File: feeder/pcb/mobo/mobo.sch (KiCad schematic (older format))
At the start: 43 parts, among them J1 SPRING_FINGER_INTERFACE, J3 SWD_10, M1 DRIVE_MOTOR, M2 PEEL_MOTOR, SW1 BUTTON_1, SW2 BUTTON_2, SW3 RESET_BUTTON, SW4 TAPE_DETECT, SW5 FILM_TENSION, U1 STM32F030K6Tx, U2 VCNT2020, U3 MAX3485, U4 DRV8833PW, U5 AP1117-33, Y1 Crystal_GND24_Small

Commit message: layout and routing done, silkscreen placed. passing drc.
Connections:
- net FILM_TENSION: now also SW5.3 (C); no longer SW5.2 (B)
- net GND: now also SW4.1 (A), SW5.1 (A); no longer SW4.3 (C), SW5.3 (C)
- net LED2: no longer U1.18 (PA8)
- net SLOT_DETECT: no longer U1.7 (PA1)
- net TAPE_DETECT: now also SW4.3 (C); no longer SW4.2 (B)
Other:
- moved on the sheet: SW4, SW5
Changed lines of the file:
@@
 L Switch:SW_SPDT SW4
 U 1 1 5DC9EA90
-P 4000 7050
-F 0 "SW4" H 4000 7335 50  0000 C CNN
-F 1 "TAPE_DETECT" H 4000 7244 50  0000 C CNN
-F 2 "index:K5-1624SA-01" H 4000 7050 50  0001 C CNN
-F 3 "" H 4000 7050 50  0001 C CNN
-	1    4000 7050
-	1    0    0    -1
+P 4100 6750
+F 0 "SW4" V 4025 6925 50  0000 C CNN
+F 1 "TAPE_DETECT" V 3925 7100 50  0000 C CNN
+F 2 "index:K5-1624SA-01" H 4100 6750 50  0001 C CNN
+F 3 "" H 4100 6750 50  0001 C CNN
+	1    4100 6750
+	0    1    1    0
 $EndComp
 $Comp
@@
 	1    0    0    -1
 $EndComp
-Wire Wire Line
-	4200 7150 4400 7150
-Wire Wire Line
-	4400 7150 4400 7300
 Wire Wire Line
 	3700 7050 3750 7050
@@
 	3750 7300 3750 7050
 Connection ~ 3750 7050
-Wire Wire Line
-	3750 7050 3800 7050
 $Comp
 L Switch:SW_Push SW3
@@
 $EndComp
 Connection ~ 3850 1150
-Text GLabel 4450 2150 2    50   Input ~ 0
-LED2
 Wire Wire Line
 	3950 1150 4050 1150
@@
 Text Notes 4800 4775 0    50   ~ 0
 POWER
-Text GLabel 4450 1450 2    50   Input ~ 0
-SLOT_DETECT
 $Comp
 L stephen:TEST TP1
@@
 L Switch:SW_SPDT SW5
 U 1 1 5F6958ED
-P 4025 5650
-F 0 "SW5" H 4025 5935 50  0000 C CNN
-F 1 "FILM_TENSION" H 4025 5844 50  0000 C CNN
-F 2 "index:K5-1624SA-01" H 4025 5650 50  0001 C CNN
-F 3 "" H 4025 5650 50  0001 C CNN
-	1    4025 5650
-	1    0    0    -1
+P 4125 5350
+F 0 "SW5" V 3975 5525 50  0000 C CNN
+F 1 "FILM_TENSION" V 3875 5700 50  0000 C CNN
+F 2 "index:K5-1624SA-01" H 4125 5350 50  0001 C CNN
+F 3 "" H 4125 5350 50  0001 C CNN
+	1    4125 5350
+	0    1    1    0
 $EndComp
 $Comp
@@
 	1    0    0    -1
 $EndComp
-Wire Wire Line
-	4225 5750 4425 5750
-Wire Wire Line
-	4425 5750 4425 5900
 Wire Wire Line
 	3725 5650 3775 5650
@@
 	3775 5900 3775 5650
 Connection ~ 3775 5650
-Wire Wire Line
-	3775 5650 3825 5650
 Text GLabel 3725 5650 0    50   Input ~ 0
 FILM_TENSION
@@
 Wire Wire Line
 	2175 1850 2175 2500
+Wire Wire Line
+	4425 5550 4225 5550
+Wire Wire Line
+	4425 5550 4425 5900
+Wire Wire Line
+	4400 6950 4200 6950
+Wire Wire Line
+	4400 6950 4400 7300
+Wire Wire Line
+	3775 5650 3775 5550
+Wire Wire Line
+	3775 5550 4025 5550
+Wire Wire Line
+	4000 7050 4000 6950
+Wire Wire Line
+	3750 7050 4000 7050
 $EndSCHEMATC

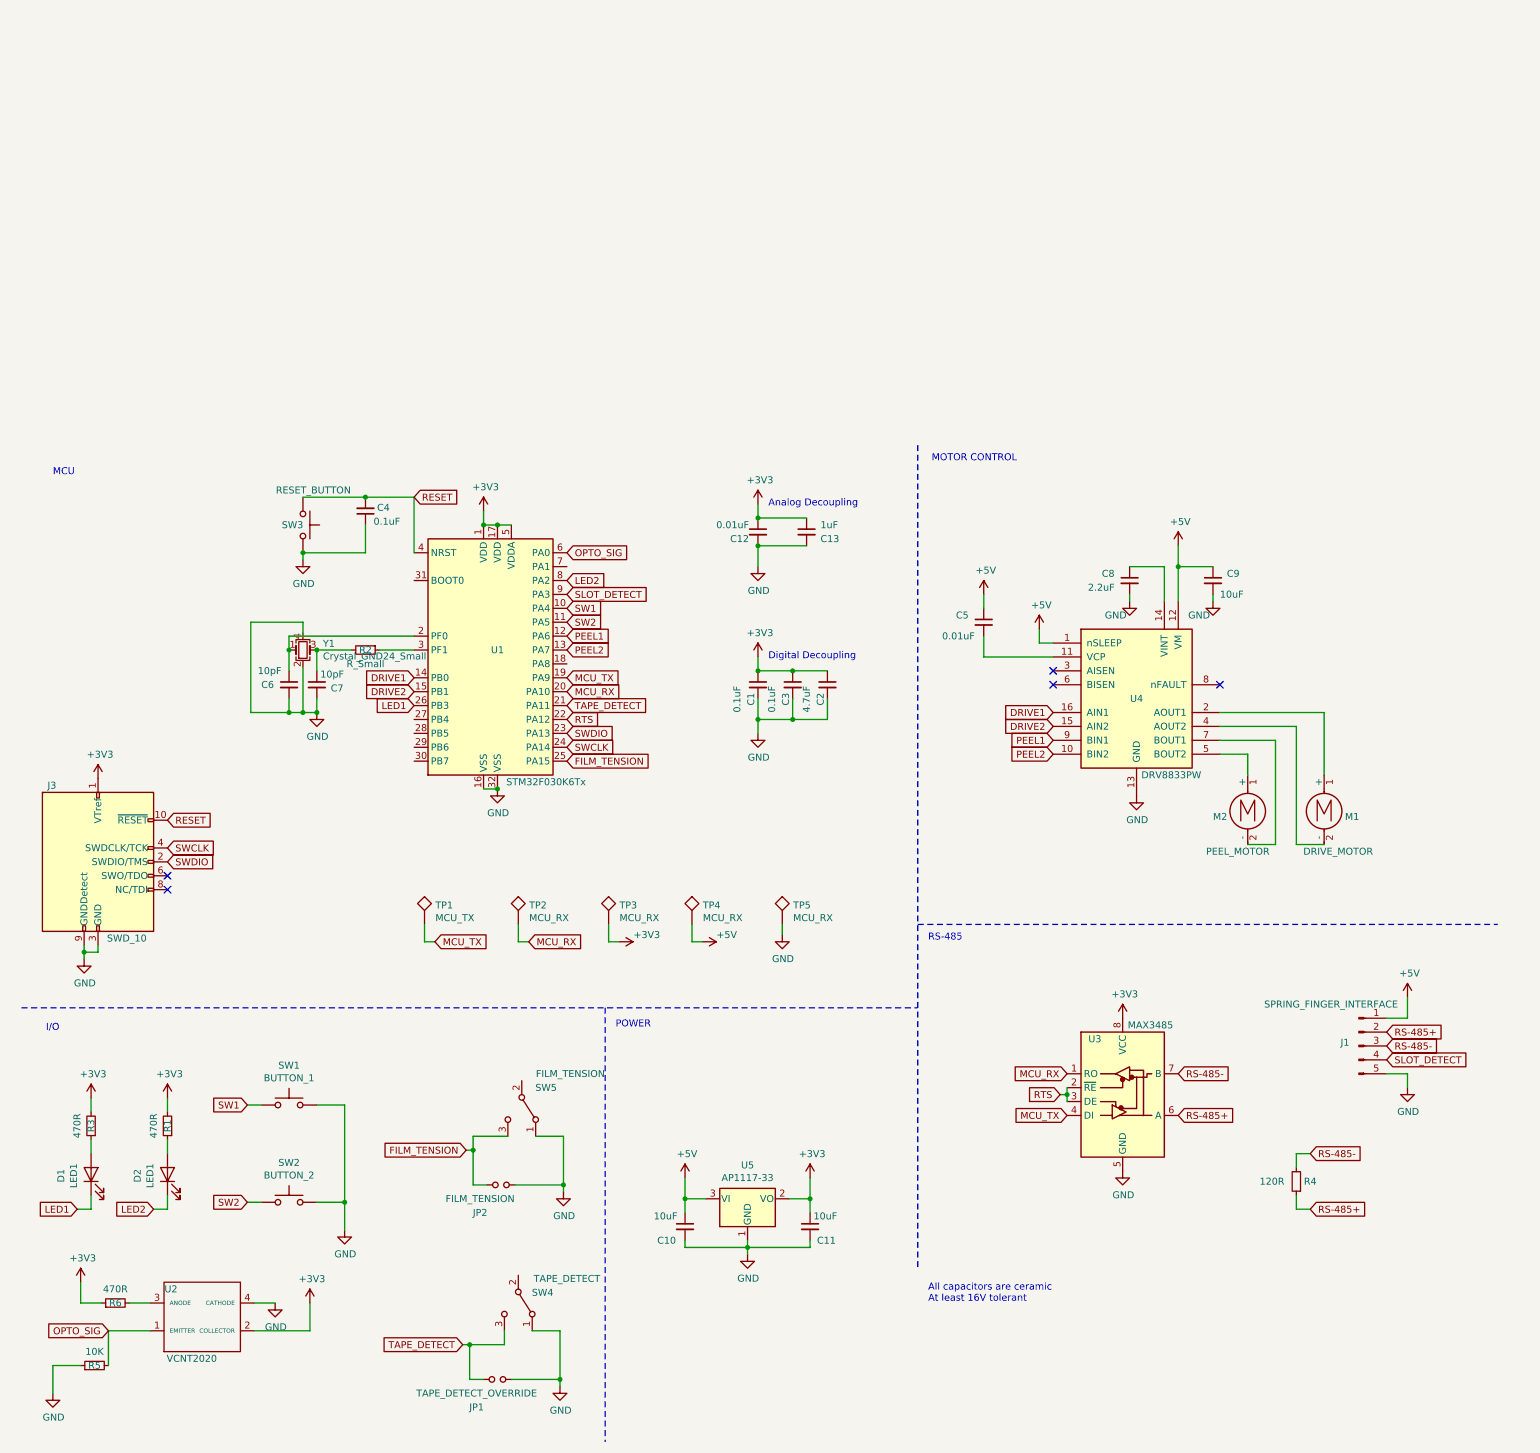
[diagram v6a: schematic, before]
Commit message: pulled DRV8833 sense pins to ground
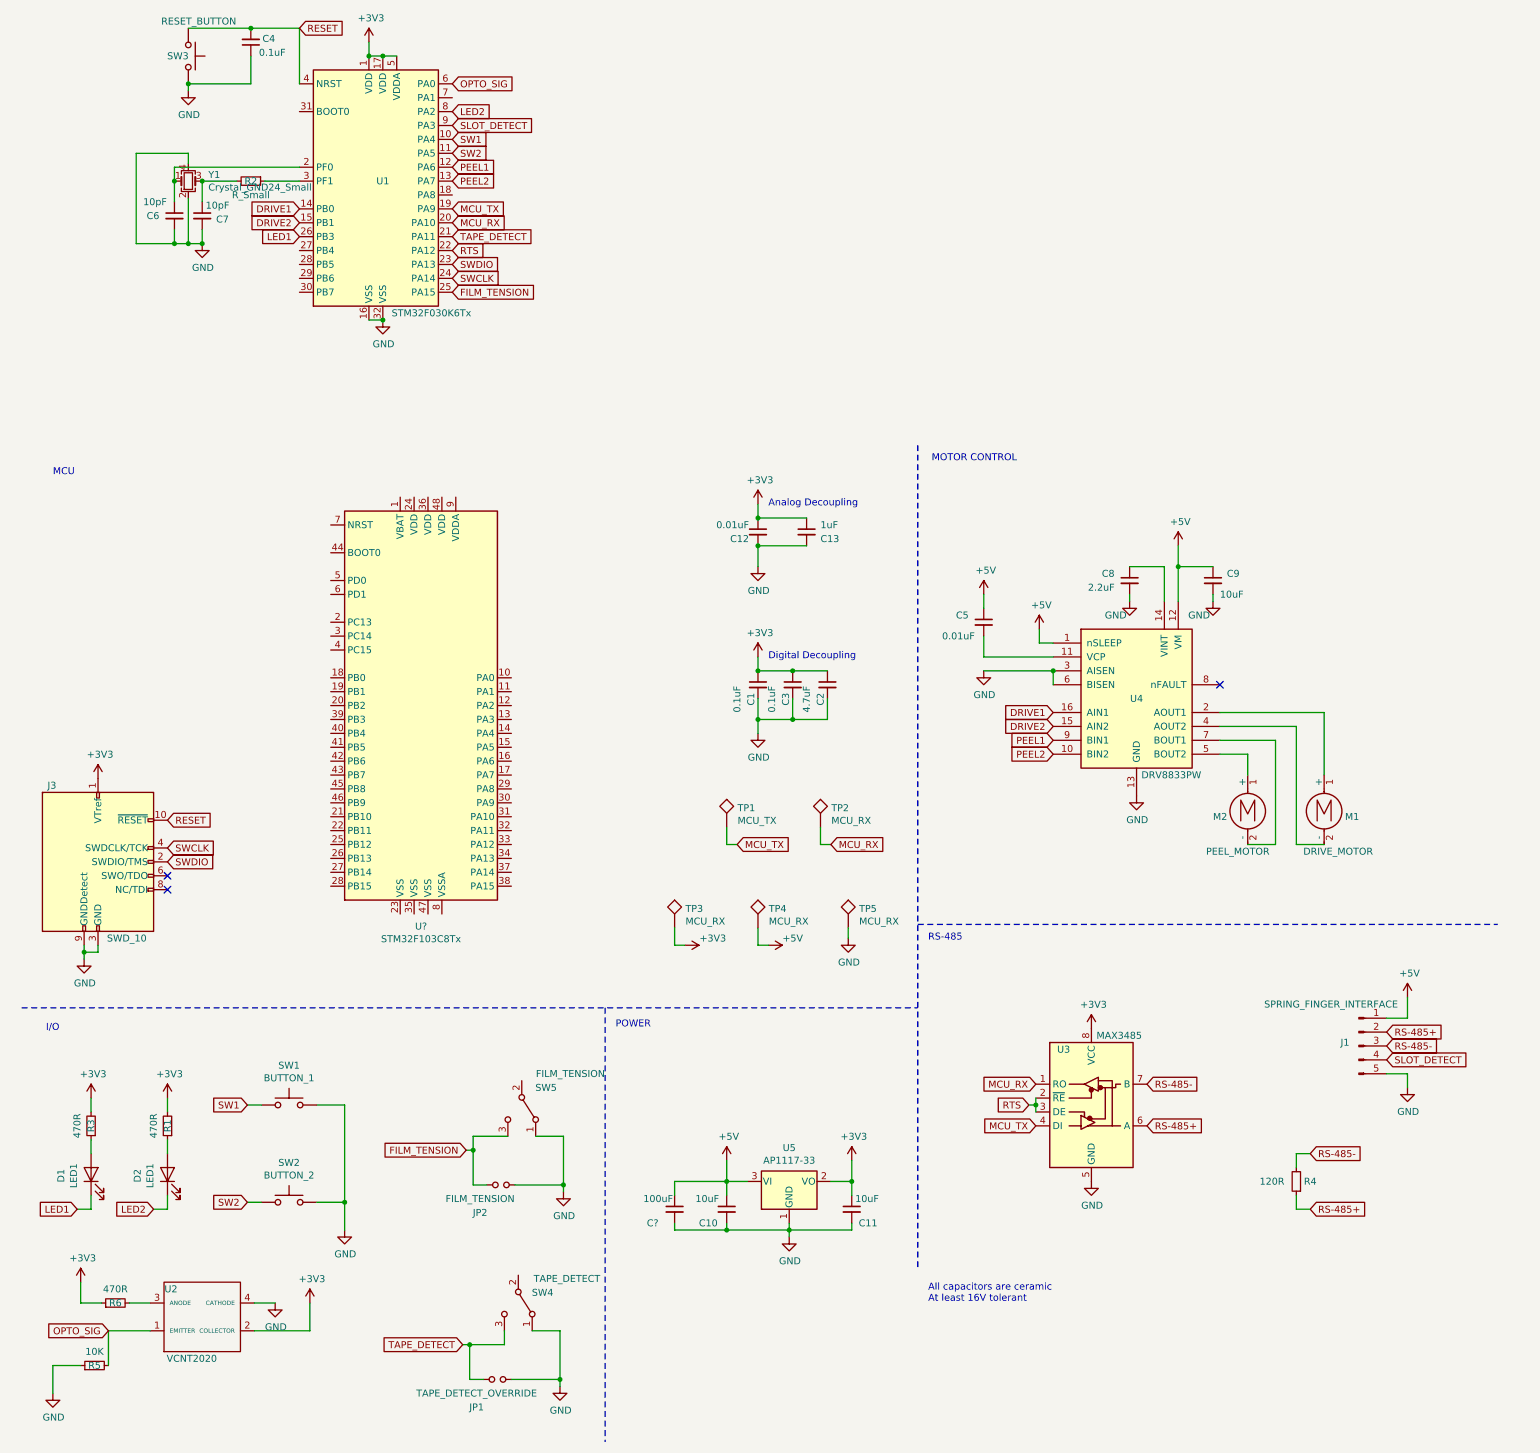
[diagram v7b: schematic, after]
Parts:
- added C?: 100uF, Capacitor_SMD:C_0805_2012Metric, symbol Device:C_Small
- added U?: STM32F103C8Tx, Package_QFP:LQFP-48_7x7mm_P0.5mm, symbol MCU_ST_STM32F1:STM32F103C8Tx
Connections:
- net +5V: now also C?.1
- net GND: now also U4.3 (AISEN), U4.6 (BISEN), C?.2
- no-connect marks 5 -> 3
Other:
- moved on the sheet: C10, C11, C4, C6, C7, R2, SW3, TP1, TP2, TP3, TP4, TP5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

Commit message: added gnd pad for DRV8833, added FTDI port, switched uC for STM32F103, fixed MAX3485 footprint, fixed SWD header footprint
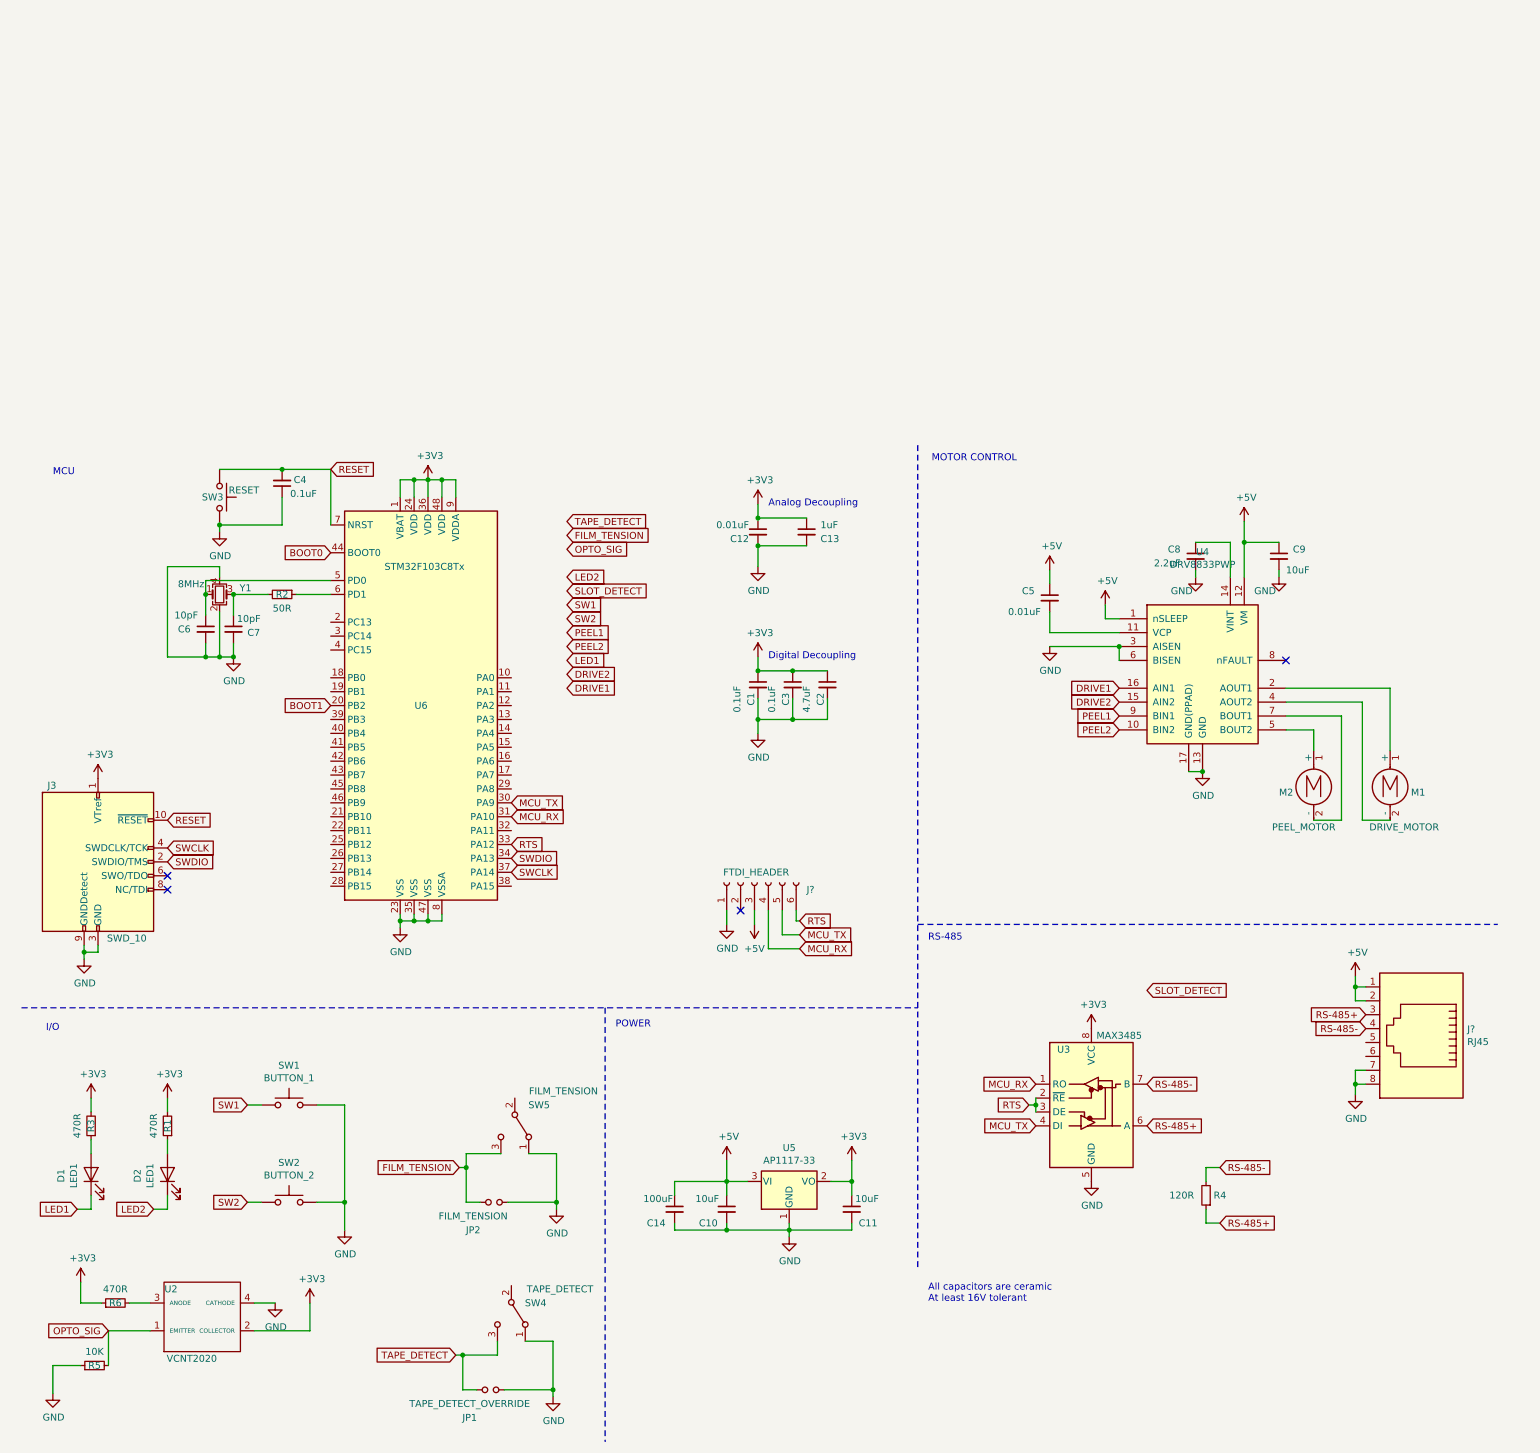
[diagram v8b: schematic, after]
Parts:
- removed J1: SPRING_FINGER_INTERFACE, index:5-pad-spring-finger-interface, symbol Connector:Conn_01x05_Male
- removed TP1: MCU_TX, TestPoint:TestPoint_Pad_D2.0mm, symbol stephen:TEST
- removed TP2, TP3, TP4, TP5: MCU_RX, TestPoint:TestPoint_Pad_D2.0mm, symbol stephen:TEST
- removed U1: STM32F030K6Tx, Package_QFP:LQFP-32_7x7mm_P0.8mm, symbol MCU_ST_STM32F0:STM32F030K6Tx
- removed U4: DRV8833PW, Package_SO:TSSOP-16_4.4x5mm_P0.65mm, symbol Driver_Motor:DRV8833PW
- added J?: FTDI_HEADER, symbol Connector:Conn_01x06_Female
- added J?: RJ45, symbol Connector:RJ45
- added U4: DRV8833PWP, Package_SO:HTSSOP-16-1EP_4.4x5mm_P0.65mm_EP3.4x5mm_Mask2.46x2.31mm_ThermalVias, symbol Driver_Motor:DRV8833PWP
- J3: footprint Connector_PinHeader_2.00mm:PinHeader_2x05_P2.00mm_Vertical_SMD -> Connector_PinHeader_1.00mm:PinHeader_2x05_P1.00mm_Vertical_SMD
- R2: value R_Small -> 50R
- SW3: value RESET_BUTTON -> RESET
- U3: footprint Package_SO:SO-8_5.3x6.2mm_P1.27mm -> Package_SO:SOIC-8_3.9x4.9mm_P1.27mm
- Y1: value Crystal_GND24_Small -> 8MHz
- gave numbers to parts that had none: 2
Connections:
- net +3V3: now also U6.1 (VBAT), U6.24 (VDD), U6.36 (VDD), U6.48 (VDD), U6.9 (VDDA)
- net +5V: now also J?.1, J?.2, J?.3 (Pin_3), U4.1 (nSLEEP), U4.12 (VM)
- net DRIVE1: now also U4.16 (AIN1)
- net DRIVE2: now also U4.15 (AIN2)
- net GND: now also U6.23 (VSS), U6.35 (VSS), U6.47 (VSS), U6.8 (VSSA), J?.1 (Pin_1), J?.7, J?.8, U4.13 (GND), U4.17 (GND(PPAD)), U4.3 (AISEN), U4.6 (BISEN)
- net MCU_RX: now also U6.31 (PA10), J?.4 (Pin_4)
- net MCU_TX: now also U6.30 (PA9), J?.5 (Pin_5)
- net PEEL1: now also U4.9 (BIN1)
- net PEEL2: now also U4.10 (BIN2)
- net RESET: now also U6.7 (NRST)
- net RS-485+: now also J?.3
- net RS-485-: now also J?.4
- net RTS: now also U6.33 (PA12), J?.6 (Pin_6)
- net SWCLK: now also U6.37 (PA14)
- net SWDIO: now also U6.34 (PA13)
- net at M1.1 (+): now also U4.2 (AOUT1)
- net at M1.2 (-): now also U4.4 (AOUT2)
- net at C5.2: now also U4.11 (VCP)
- net at C8.1: now also U4.14 (VINT)
- net at M2.1 (+): now also U4.5 (BOUT2)
- net at M2.2 (-): now also U4.7 (BOUT1)
- net at C6.1, Y1.1: now also U6.5 (PD0)
- net at R2.1: now also U6.6 (PD1)
- net BOOT1: now reaches U6.20 (PB2)
- net BOOT0: now reaches U6.44 (BOOT0)
- no-connect marks 3 -> 4
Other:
- moved on the sheet: C4, C5, C6, C7, C8, C9, JP1, JP2, M1, M2, R2, R4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
